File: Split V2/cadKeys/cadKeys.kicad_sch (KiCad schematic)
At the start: 40 parts

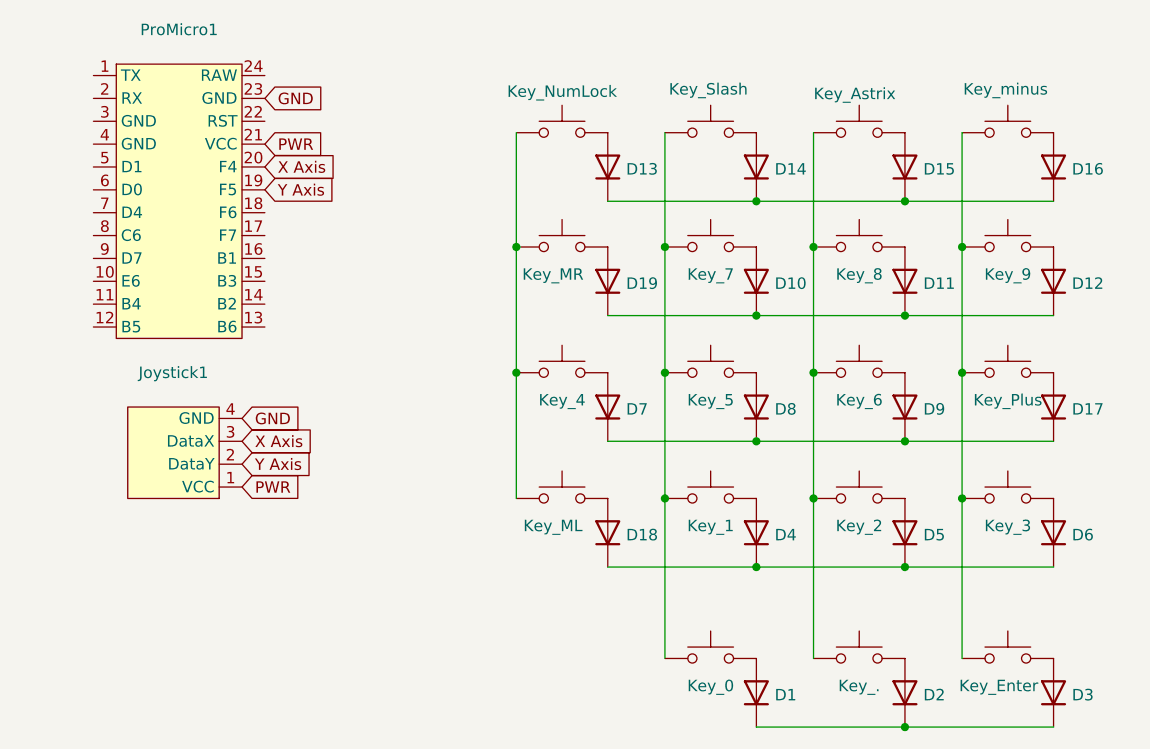
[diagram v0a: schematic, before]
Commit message: Joystick practice
got a joystick to work as a pointing device
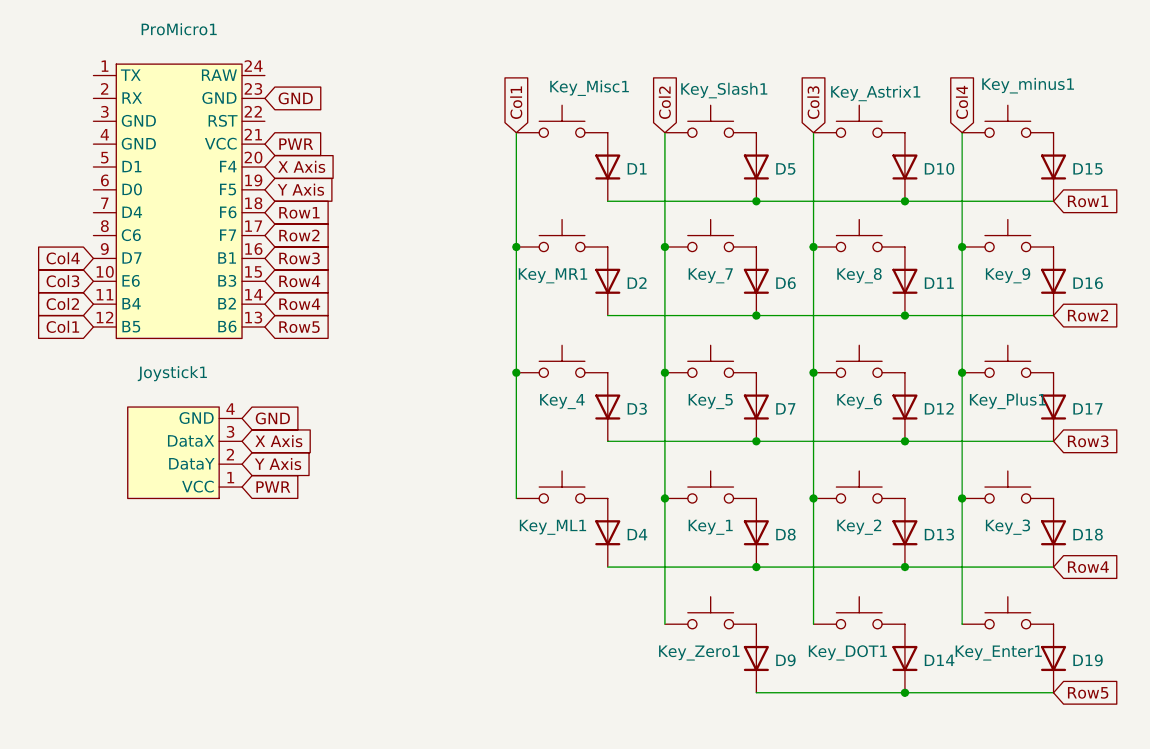
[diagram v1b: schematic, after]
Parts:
- D1: renamed from D13; footprint (none) -> Diode_SMD:D_SOD-123
- D10: renamed from D15; footprint (none) -> Diode_SMD:D_SOD-123
- D11, D17: footprint (none) -> Diode_SMD:D_SOD-123
- D12: renamed from D9; footprint (none) -> Diode_SMD:D_SOD-123
- D13: renamed from D5; footprint (none) -> Diode_SMD:D_SOD-123
- D14: renamed from D2; footprint (none) -> Diode_SMD:D_SOD-123
- D15: renamed from D16; footprint (none) -> Diode_SMD:D_SOD-123
- D16: renamed from D12; footprint (none) -> Diode_SMD:D_SOD-123
- D18: renamed from D6; footprint (none) -> Diode_SMD:D_SOD-123
- D19: renamed from D3; footprint (none) -> Diode_SMD:D_SOD-123
- D2: renamed from D19; footprint (none) -> Diode_SMD:D_SOD-123
- D3: renamed from D7; footprint (none) -> Diode_SMD:D_SOD-123
- D4: renamed from D18; footprint (none) -> Diode_SMD:D_SOD-123
- D5: renamed from D14; footprint (none) -> Diode_SMD:D_SOD-123
- D6: renamed from D10; footprint (none) -> Diode_SMD:D_SOD-123
- D7: renamed from D8; footprint (none) -> Diode_SMD:D_SOD-123
- D8: renamed from D4; footprint (none) -> Diode_SMD:D_SOD-123
- D9: renamed from D1; footprint (none) -> Diode_SMD:D_SOD-123
- Joystick1: footprint (none) -> SparkFun-KiCad-Libraries-main:joystick
- Key_1, Key_2, Key_3, Key_4, Key_5, Key_6, Key_7, Key_8, Key_9: footprint (none) -> Switch_Keyboard_Hotswap_Kailh:SW_Hotswap_Kailh_Choc_V1V2_1.00u
- Key_Astrix1: renamed from Key_Astrix; footprint (none) -> Switch_Keyboard_Hotswap_Kailh:SW_Hotswap_Kailh_Choc_V1V2_1.00u
- Key_DOT1: renamed from Key_.; footprint (none) -> Switch_Keyboard_Hotswap_Kailh:SW_Hotswap_Kailh_Choc_V1V2_1.00u
- Key_Enter1: renamed from Key_Enter; footprint (none) -> Switch_Keyboard_Hotswap_Kailh:SW_Hotswap_Kailh_Choc_V1V2_2.00u
- Key_ML1: renamed from Key_ML; footprint (none) -> Switch_Keyboard_Hotswap_Kailh:SW_Hotswap_Kailh_Choc_V1V2_1.00u
- Key_MR1: renamed from Key_MR; footprint (none) -> Switch_Keyboard_Hotswap_Kailh:SW_Hotswap_Kailh_Choc_V1V2_1.00u
- Key_Misc1: renamed from Key_NumLock; footprint (none) -> Switch_Keyboard_Hotswap_Kailh:SW_Hotswap_Kailh_Choc_V1V2_1.00u
- Key_Plus1: renamed from Key_Plus; footprint (none) -> Switch_Keyboard_Hotswap_Kailh:SW_Hotswap_Kailh_Choc_V1V2_2.00u
- Key_Slash1: renamed from Key_Slash; footprint (none) -> Switch_Keyboard_Hotswap_Kailh:SW_Hotswap_Kailh_Choc_V1V2_1.00u
- Key_Zero1: renamed from Key_0; footprint (none) -> Switch_Keyboard_Hotswap_Kailh:SW_Hotswap_Kailh_Choc_V1V2_2.00u
- Key_minus1: renamed from Key_minus; footprint (none) -> Switch_Keyboard_Hotswap_Kailh:SW_Hotswap_Kailh_Choc_V1V2_1.00u
- ProMicro1: footprint (none) -> Sparky Boards:ARDUINO_PRO_MICRO
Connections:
- net Col2: now reaches Key_1.1, Key_5.1, Key_7.1, Key_Slash1.1, Key_Zero1.1
- net Col2: now also ProMicro1.11 (B4)
- net Col3: now reaches Key_2.1, Key_6.1, Key_8.1, Key_Astrix1.1, Key_DOT1.1
- net Col3: now also ProMicro1.10 (E6)
- net Row3: now reaches D12.1 (K), D17.1 (K), D3.1 (K), D7.1 (K)
- net Row3: now also ProMicro1.16 (B1)
- net Row4: now reaches D13.1 (K), D18.1 (K), D4.1 (K), D8.1 (K)
- net Row4: now also ProMicro1.14 (B2), ProMicro1.15 (B3)
- net Row2: now reaches D11.1 (K), D16.1 (K), D2.1 (K), D6.1 (K)
- net Row2: now also ProMicro1.17 (F7)
- net Col1: now reaches Key_4.1, Key_ML1.1, Key_MR1.1, Key_Misc1.1
- net Col1: now also ProMicro1.12 (B5)
- net Col4: now reaches Key_3.1, Key_9.1, Key_Enter1.1, Key_Plus1.1, Key_minus1.1
- net Col4: now also ProMicro1.9 (D7)
- net Row5: now reaches D14.1 (K), D19.1 (K), D9.1 (K)
- net Row5: now also ProMicro1.13 (B6)
- net Row1: now reaches D1.1 (K), D10.1 (K), D15.1 (K), D5.1 (K)
- net Row1: now also ProMicro1.18 (F6)
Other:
- moved on the sheet: D14, D19, D9, Key_DOT1, Key_Enter1, Key_Zero1
